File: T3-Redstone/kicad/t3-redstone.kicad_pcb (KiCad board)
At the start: 4 copper layers, 85 x 56 mm, 5 parts, among them J1 GEMSTONE_40PIN_DISI_YUKSEK

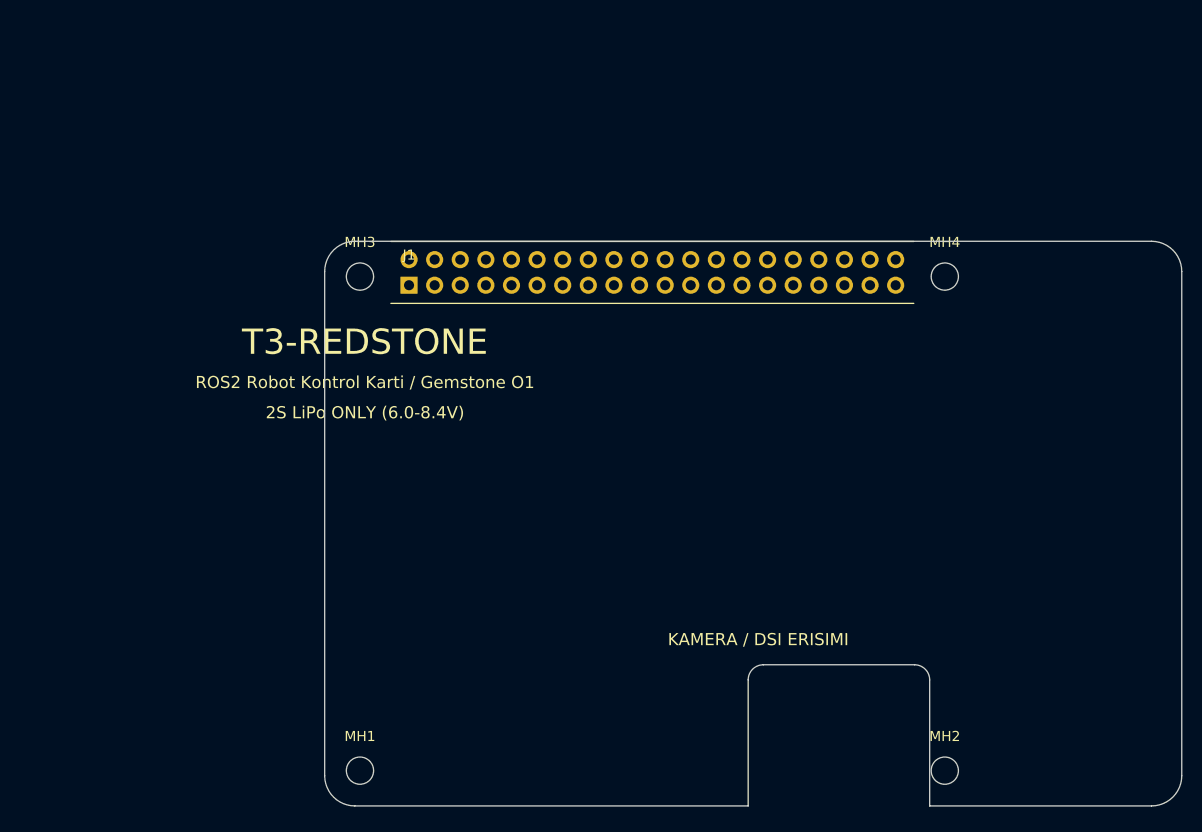
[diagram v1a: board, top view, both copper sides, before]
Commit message: Redstone: tam yerlesim, 4 katman guc duzlemleri, kirmizi maske
Board ureteci yazildi (rs_lib / rs_design / rs_emit / rs_render):

- 69 komponent, 84 net, parametrik footprint kutuphanesi (SOIC/TSSOP/SOT/
  chip/header/terminal/JST/XT60/USB-C/WROOM-1U)
- Kat plani: sol-ust USB+anten+LED, sol-orta ESP32, sol-alt guc zinciri,
  orta servo+PCA9685, sag-ust enkoder+tampon, sag motor surucu+klemens
- 4 katman: F.Cu sinyal / In1.Cu tam GND duzlemi / In2.Cu bolunmus guc
  duzlemi (VSYS, +3V3, +5V, VBAT_SW - cakismasiz) / B.Cu sinyal+GND
- Kirmizi lehim maskesi ve ENIG stackup'ta tanimli
- Guc zinciri yollari + 33 GND dikis viasi
- Yuksek akimli dugumler yol yerine yerel F.Cu bakir alani ile cozuldu

Dogrulama araclari yazildi ve temiz geciyor:
- yerlesim cakisma kontrolu (pad kutusu bazli, kenar ve kesit dahil)
- yol/pad ve yol/yol bosluk DRC'si (dikdortgen pad mesafesi)

Tasarim duzeltmeleri:
- Kesit x2 60 -> 57mm: (61.5,3.5) montaj deligine 0.1mm kaliyordu
- ESP32 WROOM-1 -> WROOM-1U + U.FL: PCB anten Gemstone'un Wi-Fi modulu ve
  metal yiginin uzerinde calismaz
- Acil stop P-FET motor suruculerin yanina tasindi, gate VSYS'e pull-up:
  ESP32 olurse motorlar durur (fail-safe)
- Shunt ana raya alindi, INA226 toplam paket akimini olcuyor
- Q1/Q2 180 donduruldu: drain/source kenarlari akis yonunde
- Buck FB bolucusu ve bootstrap kondansatoru SW dugumunden uzaklastirildi

Co-Authored-By: Claude Opus 5 <noreply@anthropic.com>
Claude-Session: https://claude.ai/code/session_01BKimLRXBxXq2q9hJZXs5Qz
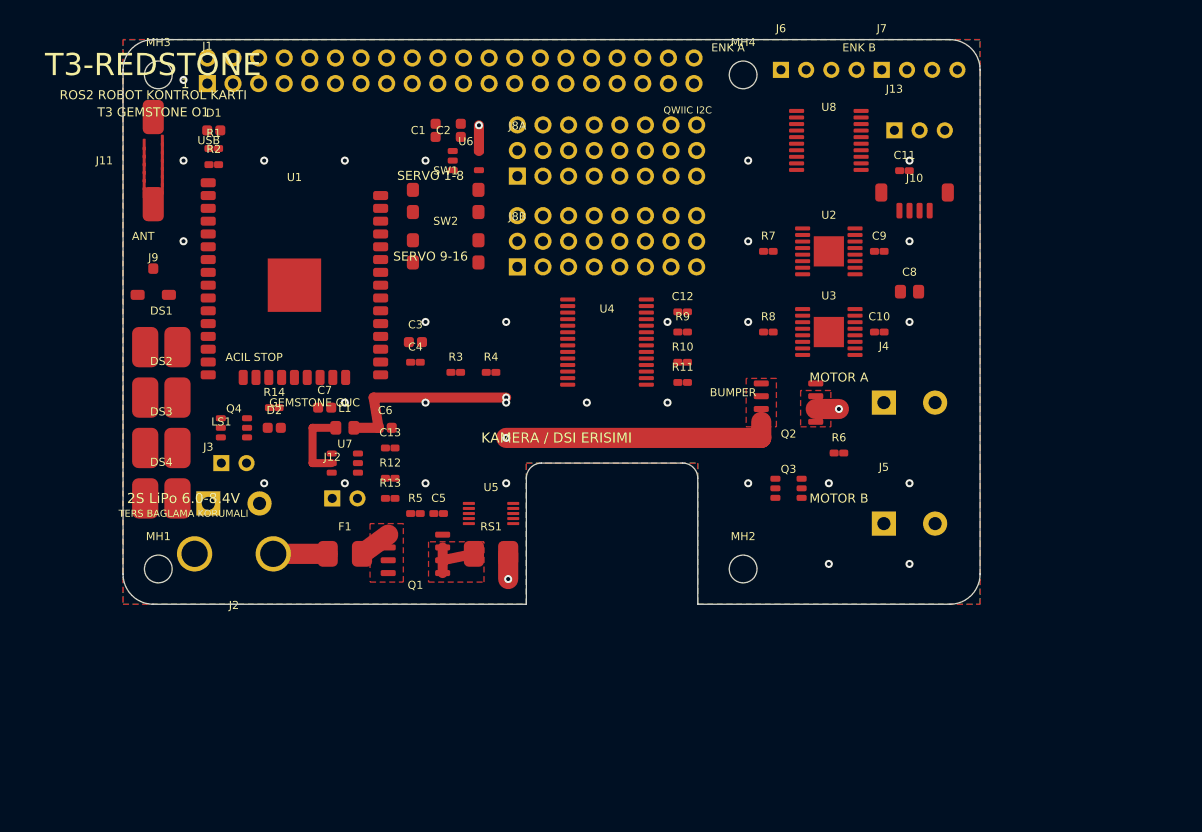
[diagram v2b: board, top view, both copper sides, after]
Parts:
- added C1: 10u, T3RS:C1, F.Cu at (61.0, 39.0)
- added C10: 100n, T3RS:C10, F.Cu at (105.0, 59.0)
- added C11: 100n, T3RS:C11, F.Cu at (107.5, 43.0)
- added C12: 100n, T3RS:C12, F.Cu at (85.5, 57.0)
- added C13: 100n, T3RS:C13, F.Cu at (56.5, 70.5)
- added C2: 10u, T3RS:C2, F.Cu at (63.5, 39.0)
- added C3: 22u, T3RS:C3, F.Cu at (59.0, 60.0)
- added C4: 100n, T3RS:C4, F.Cu at (59.0, 62.0)
- added C5: 100n, T3RS:C5, F.Cu at (61.3, 77.0)
- added C6: 22u, T3RS:C6, F.Cu at (56.0, 68.5)
- added C7: 10u, T3RS:C7, F.Cu at (50.0, 66.5)
- added C8: 100u, T3RS:C8, F.Cu at (108.0, 55.0)
- added C9: 100n, T3RS:C9, F.Cu at (105.0, 51.0)
- added D1: SS14 SOD123, T3RS:D1, F.Cu at (39.0, 39.0)
- added D2: SS14, T3RS:D2, F.Cu at (45.0, 68.5)
- added DS1: WS2812B, T3RS:DS1, F.Cu at (33.8, 60.5)
- added DS2: WS2812B, T3RS:DS2, F.Cu at (33.8, 65.5)
- added DS3: WS2812B, T3RS:DS3, F.Cu at (33.8, 70.5)
- added DS4: WS2812B, T3RS:DS4, F.Cu at (33.8, 75.5)
- added F1: 20A, T3RS:F1, F.Cu at (52.0, 81.0)
- added J10: QWIIC, T3RS:J10, F.Cu at (108.5, 47.0)
- added J11: USB-C, T3RS:J11, F.Cu at (33.0, 42.0)
- added J12: ESTOP BUTON, T3RS:J12, F.Cu at (50.8, 75.5)
- added J13: BUMPER, T3RS:J13, F.Cu at (106.5, 39.0)
- added J2: XT60 2S LiPo, T3RS:J2, F.Cu at (41.0, 81.0)
- added J3: GEMSTONE GUC, T3RS:J3, F.Cu at (38.5, 76.0)
- added J4: MOTOR A, T3RS:J4, F.Cu at (105.5, 66.0)
- added J5: MOTOR B, T3RS:J5, F.Cu at (105.5, 78.0)
- added J6: ENKODER A, T3RS:J6, F.Cu at (95.2, 33.0)
- added J7: ENKODER B, T3RS:J7, F.Cu at (105.2, 33.0)
- added J8A: SERVO 1-8, T3RS:J8A, F.Cu at (69.1, 43.5)
- added J8B: SERVO 9-16, T3RS:J8B, F.Cu at (69.1, 52.5)
- added J9: U.FL ANT, T3RS:J9, F.Cu at (33.0, 54.2)
- added L1: 4u7, T3RS:L1, F.Cu at (52.0, 68.5)
- added LS1: BUZZER, T3RS:LS1, F.Cu at (39.8, 72.0)
- added Q1: P-MOSFET, T3RS:Q1, F.Cu at (59.0, 81.0)
- added Q2: P-FET ESTOP, T3RS:Q2, F.Cu at (96.0, 66.0)
- added Q3: N-FET SOT23, T3RS:Q3, F.Cu at (96.0, 74.5)
- added Q4: N-FET SOT23, T3RS:Q4, F.Cu at (41.0, 68.5)
- added R1: 5k1, T3RS:R1, F.Cu at (39.0, 40.8)
- added R10: 4k7, T3RS:R10, F.Cu at (85.5, 62.0)
- added R11: 4k7, T3RS:R11, F.Cu at (85.5, 64.0)
- added R12: 68k, T3RS:R12, F.Cu at (56.5, 73.5)
- added R13: 10k, T3RS:R13, F.Cu at (56.5, 75.5)
- added R14: 10k, T3RS:R14, F.Cu at (45.0, 66.5)
- added R2: 5k1, T3RS:R2, F.Cu at (39.0, 42.4)
- added R3: 10k, T3RS:R3, F.Cu at (63.0, 63.0)
- added R4: 10k, T3RS:R4, F.Cu at (66.5, 63.0)
- added R5: 100k, T3RS:R5, F.Cu at (59.0, 77.0)
- added R6: 100k, T3RS:R6, F.Cu at (101.0, 71.0)
- added R7: 1k5, T3RS:R7, F.Cu at (94.0, 51.0)
- added R8: 1k5, T3RS:R8, F.Cu at (94.0, 59.0)
- added R9: 10k, T3RS:R9, F.Cu at (85.5, 59.0)
- added RS1: 2m 2W, T3RS:RS1, F.Cu at (66.5, 81.0)
- added SW1: BOOT, T3RS:SW1, F.Cu at (62.0, 46.0)
- added SW2: RESET, T3RS:SW2, F.Cu at (62.0, 51.0)
- added U1: ESP32-S3-WROOM-1U, T3RS:U1, F.Cu at (47.0, 54.4)
- added U2: DRV8874 A, T3RS:U2, F.Cu at (100.0, 51.0)
- added U3: DRV8874 B, T3RS:U3, F.Cu at (100.0, 59.0)
- added U4: PCA9685, T3RS:U4, F.Cu at (78.0, 60.0)
- added U5: INA226, T3RS:U5, F.Cu at (66.5, 77.0)
- added U6: AP2112K-3.3, T3RS:U6, F.Cu at (64.0, 42.0)
- added U7: TPS563201 5V, T3RS:U7, F.Cu at (52.0, 72.0)
- added U8: 74LVC245, T3RS:U8, F.Cu at (100.0, 40.0)
- J1: value GEMSTONE_40PIN_DISI_YUKSEK -> GEMSTONE_40P_DISI; footprint Connector_PinSocket_2.54mm:PinSocket_2x20_P2.54mm_Vertical -> T3RS:J1
- MH1: footprint MountingHole:MountingHole_2.7mm_M2.5 -> T3RS:MH1
- MH2: footprint MountingHole:MountingHole_2.7mm_M2.5 -> T3RS:MH2
- MH3: footprint MountingHole:MountingHole_2.7mm_M2.5 -> T3RS:MH3
- MH4: footprint MountingHole:MountingHole_2.7mm_M2.5 -> T3RS:MH4
- moved J1 28.3 mm to (38.4, 34.4)
- moved MH1 28.3 mm to (33.5, 82.5)
- moved MH2 28.3 mm to (91.5, 82.5)
- moved MH3 28.3 mm to (33.5, 33.5)
- moved MH4 28.3 mm to (91.5, 33.5)
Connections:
- J1 pad 10: (no net) -> HOST_RX
- J1 pad 13: (no net) -> ESTOP_STAT
- J1 pad 14: (no net) -> GND
- J1 pad 20: (no net) -> GND
- J1 pad 25: (no net) -> GND
- J1 pad 30: (no net) -> GND
- J1 pad 34: (no net) -> GND
- J1 pad 37: (no net) -> BUZZER
- J1 pad 39: (no net) -> GND
- J1 pad 6: (no net) -> GND
- J1 pad 8: (no net) -> HOST_TX
- J1 pad 9: (no net) -> GND
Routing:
- net VSYS: track 0.00 -> 29.4 mm, vias 0 -> 2
- net +5V: track 0.00 -> 18.6 mm, vias 0 -> 1
- net SW5V: track 0.00 -> 7.70 mm
- net VBAT: track 0.00 -> 5.70 mm
- net VBAT_RAW: track 0.00 -> 5.40 mm
- net VBAT_F: track 0.00 -> 3.22 mm
- net +3V3: track 0.00 -> 2.55 mm, vias 0 -> 1
- net VBAT_SW: track 0.00 -> 2.30 mm, vias 0 -> 1
- net GND: vias 0 -> 29
- added copper zone on In2.Cu, net +3V3
- added copper zone on In2.Cu, net +5V
- added copper zone on B.Cu, net GND
- added copper zone on F.Cu, net GND
- added copper zone on In1.Cu, net GND
- added copper zone on F.Cu, net VBAT
- added copper zone on F.Cu, net VBAT_F
- added copper zone on F.Cu, net VBAT_SW
- added copper zone on In2.Cu, net VBAT_SW
- added copper zone on F.Cu, net VSYS
- added copper zone on In2.Cu, net VSYS
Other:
- outline, holes or cut-outs redrawn
- rule pad_to_mask_clearance: 0 -> 0.05
- board text added: "!! DISI SOKET >=16mm - USB-A/RJ45 UZERINDEN GECER"
- board text added: "1"
- board text added: "2S LiPo 6.0-8.4V"
- board text added: "ACIL STOP"
- board text added: "ANT"
- board text added: "BUMPER"
- board text added: "ENK A"
- board text added: "ENK B"
- board text added: "GEMSTONE GUC"
- board text added: "MOTOR A"
- board text added: "MOTOR B"
- board text added: "PWM-0A/0B ve PWM-1A/1B AYNI PERIYODU PAYLASIR"
- board text added: "QWIIC I2C"
- board text added: "RJ45 h~13.5mm"
- board text added: "ROS2 ROBOT KONTROL KARTI"
- board text added: "SERVO 1-8"
- board text added: "SERVO 9-16"
- board text added: "T3 GEMSTONE O1"
- board text added: "TERS BAGLAMA KORUMALI"
- board text added: "USB"
- board text added: "USB-A x3 h~13.5mm"
- board text removed: "2S LiPo ONLY (6.0-8.4V)"
- board text removed: "RJ45 Gigabit - h~13.5mm - YUKSEK HEADER SART"
- board text removed: "ROS2 Robot Kontrol Karti / Gemstone O1"
- board text removed: "SHIELD = GEMSTONE O1 TAM BOY 85x56"
- board text removed: "USB-A x3 yigini - h~13.5mm - YUKSEK HEADER SART"

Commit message: T3-Redstone rev B: pinout duzeltmeleri, resmi footprint'ler, yonlendirme, sema
Rev A'daki entegre pinleri KiCad resmi sembol kutuphanesiyle (DRV8874 icin TI
veri sayfasiyla) tek tek karsilastirildi; kart calismazdi:
- INA226 pin tablosu tamamen yanlis (pin 7 GND'ye 3V3 -> kisa devre, SDA GND'de)
- PCA9685 LED/adres pinleri kaymis, OE servo header'ina gidiyordu
- DRV8874 pinout uydurmaydi; sarj pompasi kondansatorleri eksikti
- Acil stop P-FET'i ters: govde diyodu motoru hep besliyordu
- Host UART TX<->TX; ESP32 enkoder/bumper/LED/estop pinleri pin planina aykiri
- WS2812 LED'lerin VDD/GND'si bagsizdi; BEC 6.0V veriyordu; D1/D2 tersti
- XT60 adimi 7.8 mm cizilmisti, WROOM-1U footprint'i yanlisti
Ayrinti: docs/05-revB-degisiklikler.md

Uretim zinciri yeniden yazildi (KiCad 7 pcbnew API):
- rs_design.py tek kaynak: parca, footprint, pad->net, yerlesim, guc dagitimi
- rs_build.py: resmi kutuphane footprint'leri, 4 katman, In2 bolunmus guc,
  F.Cu guc dokumleri, kirmizi maske/ENIG stackup
- rs_route.py: Freerouting (DSN/SES), GND dikis, guc pini onarimi, DRC
- rs_sch.py: semayi uretir, semadan netlist cikarip tasarimla karsilastirir
- rs_bom.py / rs_docs.py / rs_render.py: BOM, netlist belgesi, onizleme

Donanimsal acil stop (NC buton Q3 source'unda), INA226 Kelvin baglantisi,
enkoder pull-up dizisi, USB ESD, SK6812MINI + 74AHCT1G125 eklendi.

Co-Authored-By: Claude Opus 5.5 <noreply@anthropic.com>
Claude-Session: https://claude.ai/code/session_01YQNy21SHVjiYix4RbadZre
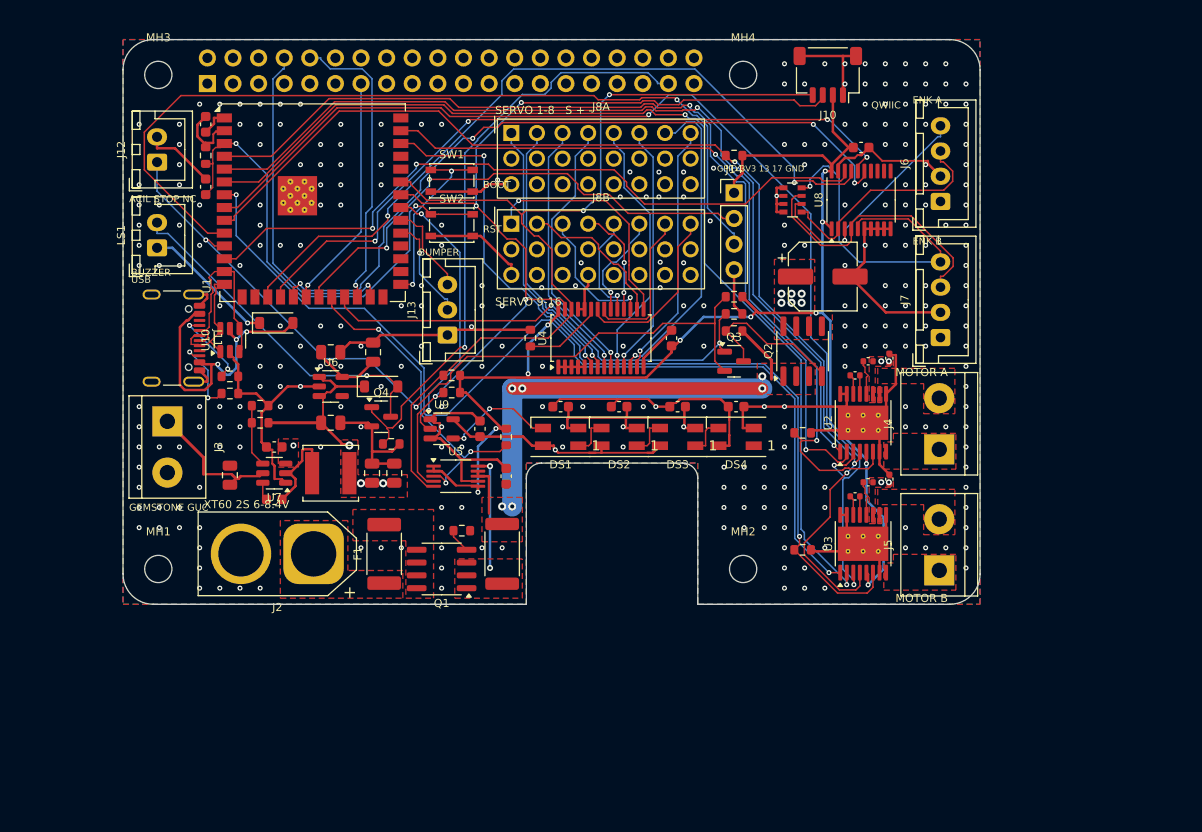
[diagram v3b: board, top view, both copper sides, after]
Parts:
- removed the J8A at (69.1, 43.5)
- removed the J8B at (69.1, 52.5)
- removed J9: U.FL ANT, T3RS:J9
- added C14: 1u, Capacitor_SMD:C_0603_1608Metric, F.Cu at (38.2, 44.6)
- added C15: 22u, Capacitor_SMD:C_0805_2012Metric, F.Cu at (54.7, 73.0)
- added C16: 100n 25V, Capacitor_SMD:C_0603_1608Metric, F.Cu at (45.0, 70.4)
- added C17: 100n, Capacitor_SMD:C_0603_1608Metric, F.Cu at (73.4, 66.4)
- added C18: 100n, Capacitor_SMD:C_0603_1608Metric, F.Cu at (79.2, 66.4)
- added C19: 100n, Capacitor_SMD:C_0603_1608Metric, F.Cu at (85.0, 66.4)
- added C20: 100n, Capacitor_SMD:C_0603_1608Metric, F.Cu at (90.8, 66.4)
- added C21: 100n, Capacitor_SMD:C_0603_1608Metric, F.Cu at (65.4, 68.6)
- added C22: 100n 16V, Capacitor_SMD:C_0402_1005Metric, F.Cu at (103.9, 61.9)
- added C23: 100n 16V, Capacitor_SMD:C_0402_1005Metric, F.Cu at (103.9, 73.9)
- added C24: 22n 50V, Capacitor_SMD:C_0402_1005Metric, F.Cu at (102.6, 63.3)
- added C25: 22n 50V, Capacitor_SMD:C_0402_1005Metric, F.Cu at (102.6, 75.3)
- added J14: GPIO, Connector_PinHeader_2.54mm:PinHeader_1x04_P2.54mm_Vertical, F.Cu at (90.6, 45.2)
- added J8A: SERVO 1-8, T3RS:Servo_3x08_P2.54mm, F.Cu at (68.5, 39.3)
- added J8B: SERVO 9-16, T3RS:Servo_3x08_P2.54mm, F.Cu at (68.5, 48.3)
- added R15: 10k, Resistor_SMD:R_0603_1608Metric, F.Cu at (68.0, 69.4)
- added R16: 100k, Resistor_SMD:R_0603_1608Metric, F.Cu at (90.6, 57.2)
- added R17: 10k, Resistor_SMD:R_0603_1608Metric, F.Cu at (90.6, 55.5)
- added RN1: 4x10k, Resistor_SMD:R_Array_Convex_4x0603, F.Cu at (96.4, 45.9)
- added U10: USBLC6-2SC6, Package_TO_SOT_SMD:SOT-23-6, F.Cu at (40.6, 59.8)
- added U9: 74AHCT1G125, Package_TO_SOT_SMD:SOT-23-5, F.Cu at (61.6, 68.6)
- C1: footprint T3RS:C1 -> Capacitor_SMD:C_0805_2012Metric
- C10: value 100n -> 100n 50V; footprint T3RS:C10 -> Capacitor_SMD:C_0402_1005Metric
- C11: footprint T3RS:C11 -> Capacitor_SMD:C_0603_1608Metric
- C12: footprint T3RS:C12 -> Capacitor_SMD:C_0603_1608Metric
- C13: footprint T3RS:C13 -> Capacitor_SMD:C_0603_1608Metric
- C2: footprint T3RS:C2 -> Capacitor_SMD:C_0805_2012Metric
- C3: footprint T3RS:C3 -> Capacitor_SMD:C_0805_2012Metric
- C4: footprint T3RS:C4 -> Capacitor_SMD:C_0603_1608Metric
- C5: footprint T3RS:C5 -> Capacitor_SMD:C_0603_1608Metric
- C6: footprint T3RS:C6 -> Capacitor_SMD:C_0805_2012Metric
- C7: value 10u -> 10u 25V; footprint T3RS:C7 -> Capacitor_SMD:C_0805_2012Metric
- C8: value 100u -> 100u 25V; footprint T3RS:C8 -> Capacitor_SMD:CP_Elec_6.3x7.7
- C9: value 100n -> 100n 50V; footprint T3RS:C9 -> Capacitor_SMD:C_0402_1005Metric
- D1: value SS14 SOD123 -> B5819W; footprint T3RS:D1 -> Diode_SMD:D_SOD-123
- D2: value SS14 -> B5819W; footprint T3RS:D2 -> Diode_SMD:D_SOD-123
- DS1: value WS2812B -> SK6812MINI; footprint T3RS:DS1 -> LED_SMD:LED_SK6812MINI_PLCC4_3.5x3.5mm_P1.75mm
- DS2: value WS2812B -> SK6812MINI; footprint T3RS:DS2 -> LED_SMD:LED_SK6812MINI_PLCC4_3.5x3.5mm_P1.75mm
- DS3: value WS2812B -> SK6812MINI; footprint T3RS:DS3 -> LED_SMD:LED_SK6812MINI_PLCC4_3.5x3.5mm_P1.75mm
- DS4: value WS2812B -> SK6812MINI; footprint T3RS:DS4 -> LED_SMD:LED_SK6812MINI_PLCC4_3.5x3.5mm_P1.75mm
- F1: footprint T3RS:F1 -> Fuse:Fuse_2512_6332Metric
- J1: value GEMSTONE_40P_DISI -> Gemstone 40P disi; footprint T3RS:J1 -> Connector_PinSocket_2.54mm:PinSocket_2x20_P2.54mm_Vertical; moved to B.Cu
- J10: footprint T3RS:J10 -> Connector_JST:JST_SH_SM04B-SRSS-TB_1x04-1MP_P1.00mm_Horizontal
- J11: footprint T3RS:J11 -> Connector_USB:USB_C_Receptacle_GCT_USB4105-xx-A_16P_TopMnt_Horizontal
- J12: value ESTOP BUTON -> ACIL STOP (NC); footprint T3RS:J12 -> Connector_JST:JST_XH_B2B-XH-A_1x02_P2.50mm_Vertical
- J13: footprint T3RS:J13 -> Connector_JST:JST_XH_B3B-XH-A_1x03_P2.50mm_Vertical
- J2: footprint T3RS:J2 -> Connector_AMASS:AMASS_XT60-F_1x02_P7.20mm_Vertical
- J3: footprint T3RS:J3 -> TerminalBlock:TerminalBlock_bornier-2_P5.08mm
- J4: footprint T3RS:J4 -> TerminalBlock:TerminalBlock_bornier-2_P5.08mm
- J5: footprint T3RS:J5 -> TerminalBlock:TerminalBlock_bornier-2_P5.08mm
- J6: footprint T3RS:J6 -> Connector_JST:JST_XH_B4B-XH-A_1x04_P2.50mm_Vertical
- J7: footprint T3RS:J7 -> Connector_JST:JST_XH_B4B-XH-A_1x04_P2.50mm_Vertical
- L1: value 4u7 -> 3u3; footprint T3RS:L1 -> Inductor_SMD:L_Sunlord_SWPA5040S
- LS1: value BUZZER -> BUZZER 5V; footprint T3RS:LS1 -> Connector_JST:JST_XH_B2B-XH-A_1x02_P2.50mm_Vertical
- MH1: footprint T3RS:MH1 -> MountingHole:MountingHole_2.7mm_M2.5
- MH2: footprint T3RS:MH2 -> MountingHole:MountingHole_2.7mm_M2.5
- MH3: footprint T3RS:MH3 -> MountingHole:MountingHole_2.7mm_M2.5
- MH4: footprint T3RS:MH4 -> MountingHole:MountingHole_2.7mm_M2.5
- Q1: value P-MOSFET -> AO4407A; footprint T3RS:Q1 -> Package_SO:SOIC-8_3.9x4.9mm_P1.27mm
- Q2: value P-FET ESTOP -> AO4407A; footprint T3RS:Q2 -> Package_SO:SOIC-8_3.9x4.9mm_P1.27mm
- Q3: value N-FET SOT23 -> AO3400A; footprint T3RS:Q3 -> Package_TO_SOT_SMD:SOT-23
- Q4: value N-FET SOT23 -> AO3400A; footprint T3RS:Q4 -> Package_TO_SOT_SMD:SOT-23
- R1: footprint T3RS:R1 -> Resistor_SMD:R_0603_1608Metric
- R10: footprint T3RS:R10 -> Resistor_SMD:R_0603_1608Metric
- R11: footprint T3RS:R11 -> Resistor_SMD:R_0603_1608Metric
- R12: value 68k -> 56k; footprint T3RS:R12 -> Resistor_SMD:R_0603_1608Metric
- R13: footprint T3RS:R13 -> Resistor_SMD:R_0603_1608Metric
- R14: footprint T3RS:R14 -> Resistor_SMD:R_0603_1608Metric
- R2: footprint T3RS:R2 -> Resistor_SMD:R_0603_1608Metric
- R3: footprint T3RS:R3 -> Resistor_SMD:R_0603_1608Metric
- R4: footprint T3RS:R4 -> Resistor_SMD:R_0603_1608Metric
- R5: footprint T3RS:R5 -> Resistor_SMD:R_0603_1608Metric
- R6: footprint T3RS:R6 -> Resistor_SMD:R_0603_1608Metric
- R7: footprint T3RS:R7 -> Resistor_SMD:R_0603_1608Metric
- R8: footprint T3RS:R8 -> Resistor_SMD:R_0603_1608Metric
- R9: footprint T3RS:R9 -> Resistor_SMD:R_0603_1608Metric
- RS1: footprint T3RS:RS1 -> Resistor_SMD:R_2512_6332Metric
- SW1: footprint T3RS:SW1 -> Button_Switch_SMD:SW_SPST_PTS810
- SW2: footprint T3RS:SW2 -> Button_Switch_SMD:SW_SPST_PTS810
- U1: value ESP32-S3-WROOM-1U -> ESP32-S3-WROOM-1U-N8R2; footprint T3RS:U1 -> RF_Module:ESP32-S3-WROOM-1U
- U2: value DRV8874 A -> DRV8874; footprint T3RS:U2 -> Package_SO:HTSSOP-16-1EP_4.4x5mm_P0.65mm_EP3.4x5mm_Mask2.46x2.31mm_ThermalVias
- U3: value DRV8874 B -> DRV8874; footprint T3RS:U3 -> Package_SO:HTSSOP-16-1EP_4.4x5mm_P0.65mm_EP3.4x5mm_Mask2.46x2.31mm_ThermalVias
- U4: value PCA9685 -> PCA9685PW; footprint T3RS:U4 -> Package_SO:TSSOP-28_4.4x9.7mm_P0.65mm
- U5: footprint T3RS:U5 -> Package_SO:VSSOP-10_3x3mm_P0.5mm
- U6: footprint T3RS:U6 -> Package_TO_SOT_SMD:SOT-23-5
- U7: value TPS563201 5V -> TPS563201; footprint T3RS:U7 -> Package_TO_SOT_SMD:SOT-23-6
- U8: footprint T3RS:U8 -> Package_SO:TSSOP-20_4.4x6.5mm_P0.65mm
- moved DS4 57.3 mm to (90.8, 69.4), turned to 180 degrees
- moved DS3 51.2 mm to (85.0, 69.4), turned to 180 degrees
- moved J13 48.8 mm to (62.2, 59.3), turned to 90 degrees
- moved DS2 45.6 mm to (79.2, 69.4), turned to 180 degrees
- moved DS1 40.6 mm to (73.4, 69.4), turned to 180 degrees
- moved J12 37.6 mm to (33.4, 42.1), turned to 90 degrees
- moved R3 32.8 mm to (38.2, 41.5), turned to 90 degrees
- moved R4 32.3 mm to (90.6, 41.5)
- moved C4 31.5 mm to (38.2, 38.4), turned to -90 degrees
- moved C1 30.8 mm to (50.6, 68.0), turned to 0 degrees
- moved J7 27.2 mm to (111.1, 59.5), turned to 90 degrees
- moved U6 26.1 mm to (50.6, 64.4)
- moved C2 25.5 mm to (50.6, 61.0), turned to 0 degrees
- moved R10 23.1 mm to (62.6, 65.0)
- moved R11 22.9 mm to (62.6, 63.3)
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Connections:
- D1 pad 1: +5V_USB -> +5V
- D1 pad 2: +5V -> +5V_USB
- D2 pad 1: BUZZER_DRV -> +5V
- D2 pad 2: +3V3 -> BUZZER_DRV
- DS1 pad 1: LED_DATA -> LED_D1
- DS1 pad 2: LED_D1 -> GND
- DS2 pad 1: LED_D1 -> LED_D2
- DS2 pad 2: LED_D2 -> GND
- DS3 pad 1: LED_D2 -> LED_D3
- DS3 pad 2: LED_D3 -> GND
- DS4 pad 1: LED_D3 -> LED_D4
- DS4 pad 2: LED_D4 -> GND
- J12 pad 1: ESTOP_BTN -> ESTOP_LOOP
- LS1 pad 1: +3V3 -> +5V
- Q2 pad 1: VBAT_SW -> VSYS
- Q2 pad 2: VBAT_SW -> VSYS
- Q2 pad 3: VBAT_SW -> VSYS
- Q2 pad 5: VSYS -> VBAT_SW
- Q2 pad 6: VSYS -> VBAT_SW
- Q2 pad 7: VSYS -> VBAT_SW
- Q2 pad 8: VSYS -> VBAT_SW
- Q3 pad 2: GND -> ESTOP_LOOP
- SW1 pad 2: BOOT_BTN -> GND
- SW2 pad 2: EN -> GND
- U1 pad 10: ENC_B1 -> GPIO17
- U1 pad 11: ENC_A2 -> ESTOP_LOOP
- U1 pad 15: BOOT_STRAP -> (no net)
- U1 pad 17: ENC_B2 -> ENC_B1
- U1 pad 18: GPIO10 -> ENC_A2
- U1 pad 19: GPIO11 -> ENC_B2
- U1 pad 21: SPARE2 -> GPIO13
- U1 pad 22: SPARE3 -> PWR_ALERT
- U1 pad 24: HOST_TX -> HOST_RX
- U1 pad 25: HOST_RX -> HOST_TX
- U1 pad 28: SPARE5 -> (no net)
- U1 pad 29: BUMP2 -> (no net)
- U1 pad 30: BUMP1 -> (no net)
- U1 pad 31: LED_DATA -> BUMP1
- U1 pad 32: ESTOP_BTN -> BUMP2
- U1 pad 33: SPARE4 -> LED_DATA
- U1 pad 36: DBG_RX -> (no net)
- U1 pad 37: DBG_TX -> (no net)
- U2 pad 1: IPROPI_A -> MA_EN
- U2 pad 10: GND -> OUTA2
- U2 pad 11: GND -> VBAT_SW
- U2 pad 12: OUTA2 -> VCP_A
- U2 pad 13: OUTA1 -> CPH_A
- U2 pad 14: VBAT_SW -> CPL_A
- U2 pad 15: VBAT_SW -> GND
- U2 pad 16: OUTA1 -> GND
- U2 pad 2: DRV_nSLEEP -> MA_PH
- U2 pad 3: MA_EN -> DRV_nSLEEP
- U2 pad 4: MA_PH -> DRV_nFAULT
- U2 pad 5: DRV_nFAULT -> +3V3
- U2 pad 6: GND -> IPROPI_A
- U2 pad 7: +3V3 -> GND
- U2 pad 8: GND -> OUTA1
- U2 pad 9: OUTA2 -> GND
- U3 pad 1: IPROPI_B -> MB_EN
- U3 pad 10: GND -> OUTB2
- U3 pad 11: GND -> VBAT_SW
- U3 pad 12: OUTB2 -> VCP_B
- U3 pad 13: OUTB1 -> CPH_B
- U3 pad 14: VBAT_SW -> CPL_B
- U3 pad 15: VBAT_SW -> GND
- U3 pad 16: OUTB1 -> GND
- U3 pad 2: DRV_nSLEEP -> MB_PH
- U3 pad 3: MB_EN -> DRV_nSLEEP
- U3 pad 4: MB_PH -> DRV_nFAULT
- U3 pad 5: DRV_nFAULT -> +3V3
- U3 pad 6: GND -> IPROPI_B
- U3 pad 7: +3V3 -> GND
- U3 pad 8: GND -> OUTB1
- U3 pad 9: OUTB2 -> GND
- U4 pad 10: SERVO4 -> SERVO5
- U4 pad 11: SERVO5 -> SERVO6
- U4 pad 12: SERVO6 -> SERVO7
- U4 pad 13: SERVO7 -> SERVO8
- U4 pad 15: SERVO8 -> SERVO9
- U4 pad 16: SERVO9 -> SERVO10
- U4 pad 17: SERVO10 -> SERVO11
- U4 pad 18: SERVO11 -> SERVO12
- U4 pad 19: SERVO12 -> SERVO13
- U4 pad 20: SERVO13 -> SERVO14
- U4 pad 21: SERVO14 -> SERVO15
- U4 pad 22: SERVO15 -> SERVO16
- U4 pad 23: SERVO16 -> OE_N
- U4 pad 24: OE_N -> GND
- U4 pad 6: GND -> SERVO1
- U4 pad 7: SERVO1 -> SERVO2
- U4 pad 8: SERVO2 -> SERVO3
- U4 pad 9: SERVO3 -> SERVO4
- U5 pad 1: VBAT -> +3V3
- U5 pad 10: +3V3 -> VBAT
- U5 pad 2: VSYS -> +3V3
- U5 pad 4: GND -> I2C_SDA
- U5 pad 6: I2C_SDA -> +3V3
- U5 pad 7: +3V3 -> GND
- U5 pad 8: GND -> VSYS
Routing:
- net GND: track 0.00 -> 236.0 mm, vias 29 -> 287
- net +3V3: track 2.55 -> 156.0 mm, vias 1 -> 11
- net DRV_nSLEEP: track 0.00 -> 114.2 mm, vias 0 -> 3
- net DRV_nFAULT: track 0.00 -> 113.3 mm, vias 0 -> 3
- net MB_PH: track 0.00 -> 104.4 mm, vias 0 -> 2
- net MB_EN: track 0.00 -> 98.2 mm, vias 0 -> 2
- net MA_PH: track 0.00 -> 94.2 mm, vias 0 -> 2
- net I2C_SCL: track 0.00 -> 93.7 mm, vias 0 -> 2
- net I2C_SDA: track 0.00 -> 92.2 mm, vias 0 -> 4
- net MA_EN: track 0.00 -> 90.8 mm, vias 0 -> 2
- net GPIO17: track 0.00 -> 85.9 mm, vias 0 -> 1
- net IPROPI_B: track 0.00 -> 83.5 mm, vias 0 -> 2
- net ESTOP_LOOP: track 0.00 -> 81.2 mm, vias 0 -> 2
- net IPROPI_A: track 0.00 -> 78.2 mm, vias 0 -> 2
- net ENC_B1: track 0.00 -> 75.9 mm, vias 0 -> 2
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- added copper zone on F.Cu, net +5V
- added copper zone on F.Cu, net OUTA1
- added copper zone on F.Cu, net OUTA2
- added copper zone on F.Cu, net OUTB1
- added copper zone on F.Cu, net OUTB2
- added copper zone on F.Cu, net VBAT_RAW
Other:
- rule pad_to_mask_clearance: 0.05 -> 0
- board text added: "+"
- board text added: "2S LiPo 6.0-8.4V - ters baglama korumali"
- board text added: "40-pin disi soket >= 16 mm (USB-A/RJ45 uzerinden gecer)"
- board text added: "ACIL STOP NC"
- board text added: "Acil stop NC: J12'ye buton ya da kopru takilmazsa motorlar calismaz"
- board text added: "BOOT"
- board text added: "BUZZER"
- board text added: "Bu yuze komponent KONMAZ (soket haric)"
- board text added: "GPIO 3V3 13 17 GND"
- board text added: "QWIIC"
- board text added: "RJ45 h~13.5mm (Gemstone)"
- board text added: "ROS 2 robot kontrol karti / T3 Gemstone O1"
- board text added: "RST"
- board text added: "SERVO 1-8 S + -"
- board text added: "T3-REDSTONE rev B"
- board text added: "USB-A x3 h~13.5mm (Gemstone)"
- board text added: "XT60 2S 6-8.4V"
- board text removed: "!! DISI SOKET >=16mm - USB-A/RJ45 UZERINDEN GECER"
- board text removed: "1"
- board text removed: "2S LiPo 6.0-8.4V"
- board text removed: "ACIL STOP"
- board text removed: "ANT"
- board text removed: "KAMERA / DSI ERISIMI"
- board text removed: "PWM-0A/0B ve PWM-1A/1B AYNI PERIYODU PAYLASIR"
- board text removed: "QWIIC I2C"
- board text removed: "RJ45 h~13.5mm"
- board text removed: "ROS2 ROBOT KONTROL KARTI"
- board text removed: "SERVO 1-8"
- board text removed: "T3 GEMSTONE O1"
- board text removed: "T3-REDSTONE"
- board text removed: "TERS BAGLAMA KORUMALI"
- board text removed: "USB-A x3 h~13.5mm"
